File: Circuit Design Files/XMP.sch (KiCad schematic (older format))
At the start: 18 parts, among them K1 CONN_3, P1 CONN_2

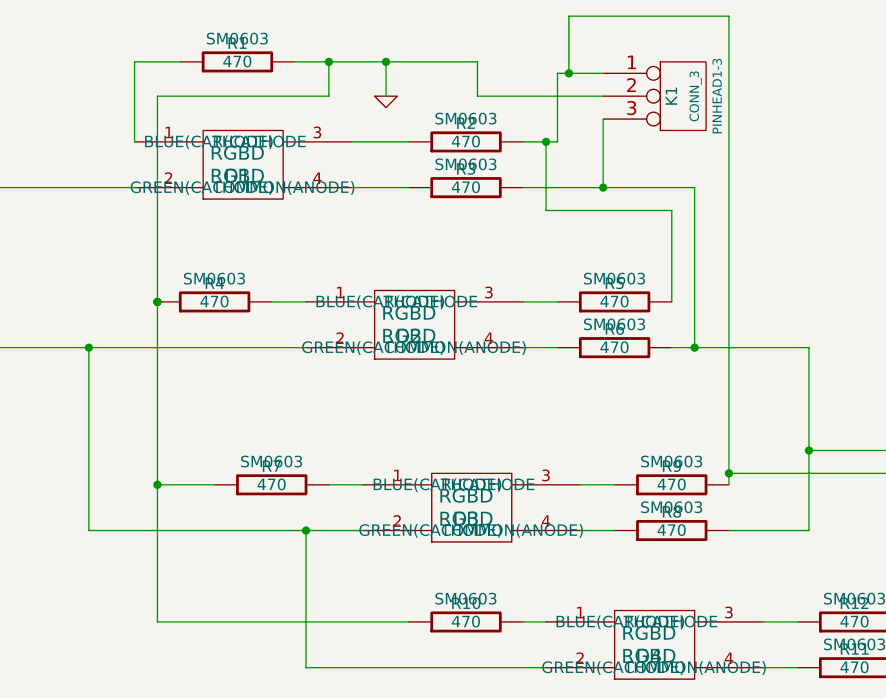
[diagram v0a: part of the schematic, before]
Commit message: Updated circuit designs with the part number of the RGB LED in use.
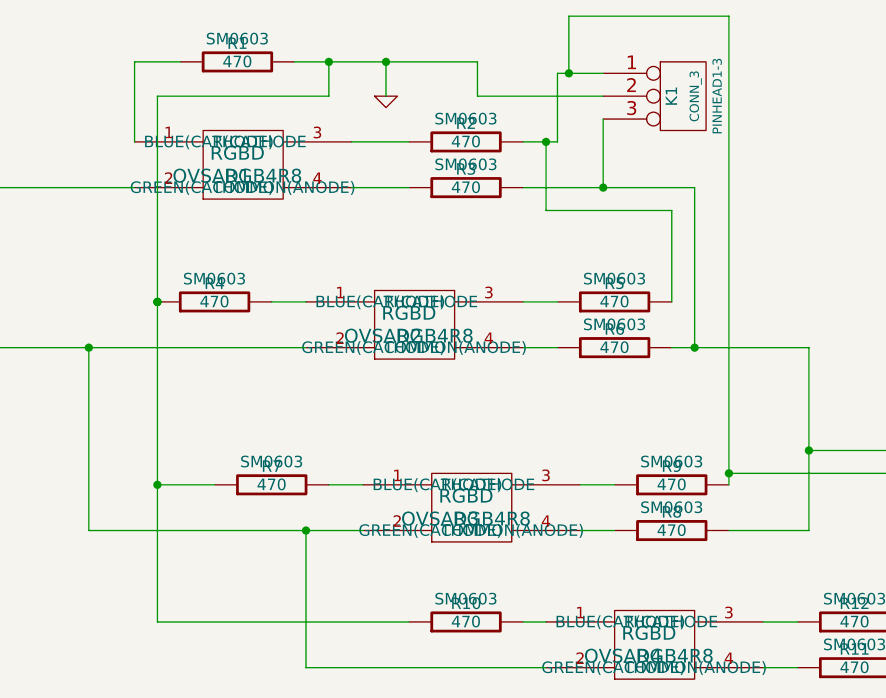
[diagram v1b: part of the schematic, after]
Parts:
- D1, D2, D3, D4: value RGBD -> OVSARGB4R8
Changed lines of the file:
@@
-EESchema Schematic File Version 2  date Fri 19 Apr 2013 07:35:14 AM EDT
+EESchema Schematic File Version 2  date Fri 19 Apr 2013 10:32:41 AM EDT
 LIBS:power
 LIBS:device
@@
 Sheet 1 1
 Title ""
-Date "13 apr 2013"
+Date "19 apr 2013"
 Rev ""
 Comp ""
@@
 P 6050 4250
 F 0 "D4" H 6050 4250 60  0000 C CNN
-F 1 "RGBD" H 6050 4250 60  0000 C CNN
+F 1 "OVSARGB4R8" H 6050 4250 60  0000 C CNN
 F 2 "RGBD" H 6050 4350 60  0000 C CNN
 	1    6050 4250
@@
 P 5250 3650
 F 0 "D3" H 5250 3650 60  0000 C CNN
-F 1 "RGBD" H 5250 3650 60  0000 C CNN
+F 1 "OVSARGB4R8" H 5250 3650 60  0000 C CNN
 F 2 "RGBD" H 5250 3750 60  0000 C CNN
 	1    5250 3650
@@
 P 5000 2850
 F 0 "D2" H 5000 2850 60  0000 C CNN
-F 1 "RGBD" H 5000 2850 60  0000 C CNN
+F 1 "OVSARGB4R8" H 5000 2850 60  0000 C CNN
 F 2 "RGBD" H 5000 2950 60  0000 C CNN
 	1    5000 2850
@@
 P 4250 2150
 F 0 "D1" H 4250 2150 60  0000 C CNN
-F 1 "RGBD" H 4250 2150 60  0000 C CNN
+F 1 "OVSARGB4R8" H 4250 2150 60  0000 C CNN
 F 2 "RGBD" H 4250 2250 60  0000 C CNN
 	1    4250 2150

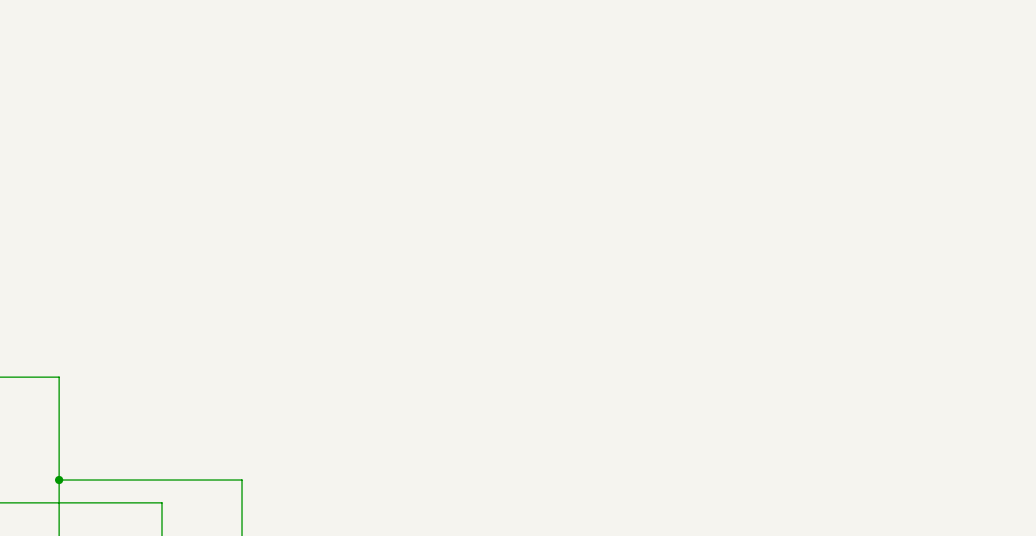
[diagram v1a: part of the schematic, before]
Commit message: Added License information to documents.
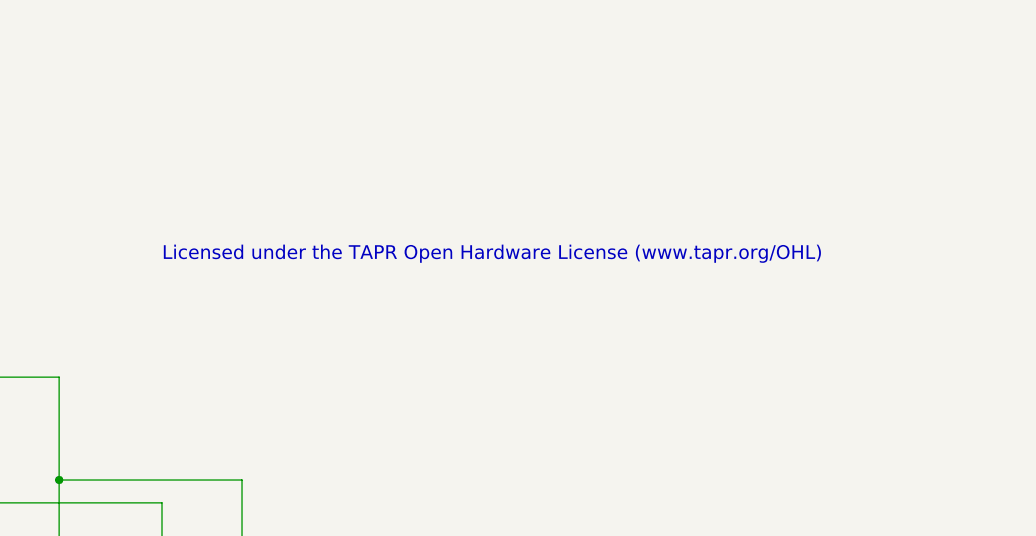
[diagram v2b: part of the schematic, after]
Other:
- note added: "Licensed under the TAPR Open Hardware License (www.tapr.org/OHL)"
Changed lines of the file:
@@
-EESchema Schematic File Version 2  date Fri 19 Apr 2013 10:32:41 AM EDT
+EESchema Schematic File Version 2  date Sun 21 Apr 2013 05:50:57 PM EDT
 LIBS:power
 LIBS:device
@@
 LIBS:valves
 LIBS:rgbd
-LIBS:XMP-cache
 EELAYER 25  0
 EELAYER END
@@
 Sheet 1 1
 Title ""
-Date "19 apr 2013"
+Date "21 apr 2013"
 Rev ""
 Comp ""
@@
 Comment4 ""
 $EndDescr
+Text Notes 7200 2400 0    60   ~ 0
+Licensed under the TAPR Open Hardware License (www.tapr.org/OHL)
 Connection ~ 6400 3450
 Wire Wire Line

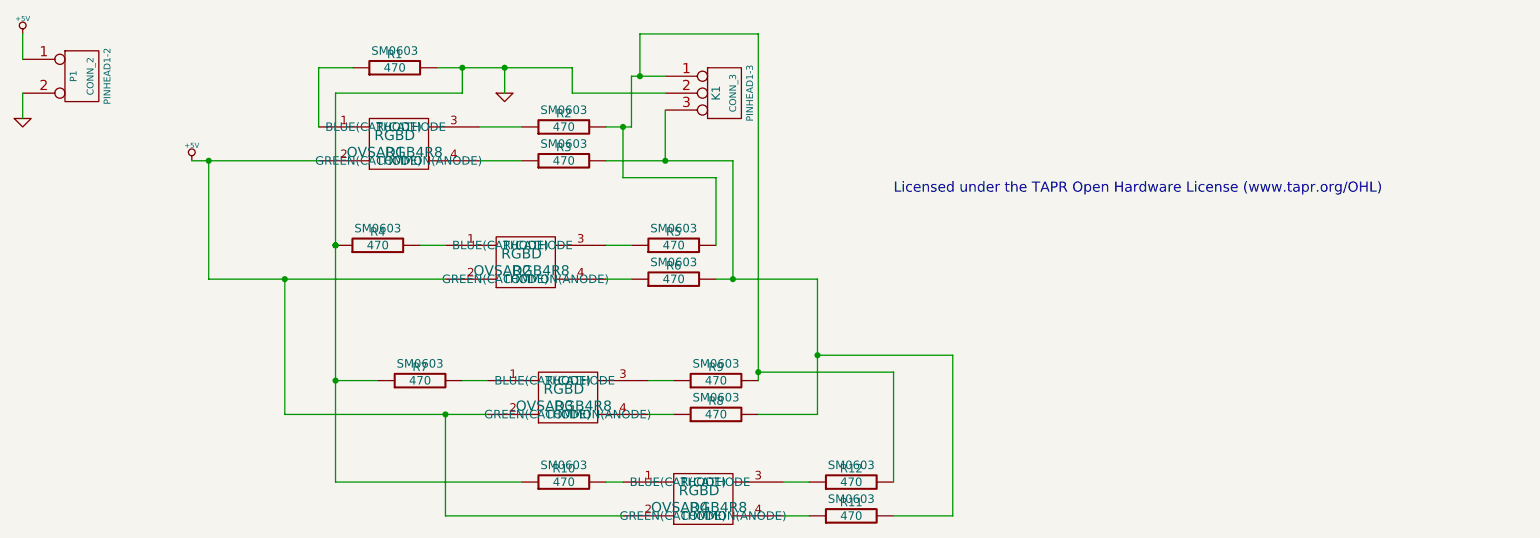
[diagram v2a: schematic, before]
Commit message: Updated circuit design files to fix issues with labeling (among other things)
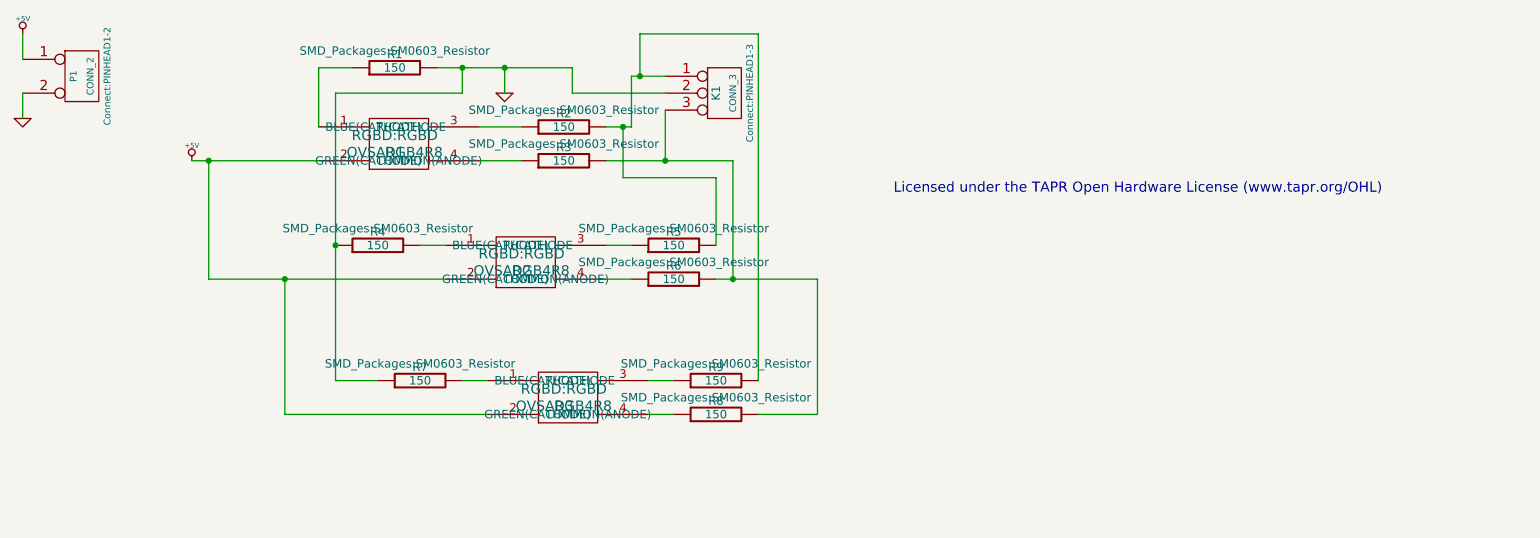
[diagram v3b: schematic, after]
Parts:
- removed D4: OVSARGB4R8, RGBD, symbol RGBD
- removed R10, R11, R12: 470, SM0603, symbol R
- D1, D2, D3: footprint RGBD -> RGBD:RGBD
- K1: footprint PINHEAD1-3 -> Connect:PINHEAD1-3
- P1: footprint PINHEAD1-2 -> Connect:PINHEAD1-2
- R1, R2, R3, R4, R5, R6, R7, R8, R9: value 470 -> 150; footprint SM0603 -> SMD_Packages:SM0603_Resistor
